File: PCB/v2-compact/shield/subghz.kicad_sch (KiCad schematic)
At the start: 0 parts

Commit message: Schematics: sub-GHz trio sheet (CC1200 + SX1262 + CC1101) + fixes
- 05_SubGHz (A3): CC1200 and SX1262 (bare QFN) with SPI, control, power,
  crystals and decoupling wired; CC1101 as an 8-pin module. Chip-selects come
  from the MCP23S17 (CC1200_CS, SX1262_NSS, CC1101_CSN), SX1262 BUSY direct on
  the C5. RF front-ends (PA/LNA/RFO/RFI -> match -> SMA) flagged for the RF pass.
  Verified: SPI_SCK now reaches all nine SPI devices.
- Fix the Espressif symbol-lib-table path to Windows form (was Git-Bash /d/...).
- Add A3 page support to the generator.
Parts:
- added C80, C81: 10pF, Capacitor_SMD:C_0402_1005Metric, symbol Device:C
- added C82, C83, C86, C87, C88: 100nF, Capacitor_SMD:C_0402_1005Metric, symbol Device:C
- added C84, C85: 12pF, Capacitor_SMD:C_0402_1005Metric, symbol Device:C
- added R80: 56k, Resistor_SMD:R_0402_1005Metric, symbol Device:R
- added U4: CC1101, symbol SnowOwl:CC1101_Module
- added U5: CC1200RHBR, Package_DFN_QFN:QFN-32-1EP_5x5mm_P0.5mm_EP3.45x3.45mm, symbol RF:CC1200
- added U6: SX1262IMLTRT, Package_DFN_QFN:QFN-24-1EP_4x4mm_P0.5mm_EP2.6x2.6mm, symbol RF:SX1262IMLTRT
- added Y60: 40MHz, Crystal:Crystal_SMD_3225-4Pin_3.2x2.5mm, symbol Device:Crystal
- added Y61: 32MHz, Crystal:Crystal_SMD_3225-4Pin_3.2x2.5mm, symbol Device:Crystal
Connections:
- new net +3V3: C82.1, C86.1, C88.1, U4.2 (VCC), U5.1 (VDD_GUARD), U5.12 (DVDD), U5.13 (AVDD_IF), U5.15 (AVDD_RF), U5.22 (AVDD_SYNTH1), U5.25 (AVDD_PFD_CHP), U5.27 (AVDD_SYNTH2), U5.28 (AVDD_XOSC), U5.5 (DVDD), U6.1 (VDD_IN), U6.10 (VBAT), U6.11 (VBAT_IO)
- new net CC1101_CSN: U4.4 (CSN)
- new net CC1101_GDO0: U4.3 (GDO0)
- new net CC1101_GDO2: U4.7 (GDO2)
- new net CC1200_CS: U5.11 (~{CS})
- new net CC1200_GPIO0: U5.10 (GPIO0)
- new net CC1200_GPIO2: U5.4 (GPIO2)
- new net CC1200_GPIO3: U5.3 (GPIO3)
- new net CC1200_RST: U5.2 (~{RESET})
- new net CC12_DCPL_PFD: U5.26 (DCPL_PFD_CHP)
- new net CC12_DCPL_VCO: U5.21 (DCPL_VCO)
- new net CC12_DCPL_XOSC: U5.29 (DCPL_XOSC)
- new net CC12_LNA_N: U5.20 (LNA_N)
- new net CC12_LNA_P: U5.19 (LNA_P)
- new net CC12_LPF0: U5.23 (LPF0)
- new net CC12_LPF1: U5.24 (LPF1)
- new net CC12_PA: U5.17 (PA)
- new net CC12_RBIAS: R80.1, U5.14 (RBIAS)
- new net CC12_TRXSW: U5.18 (TRX_SW)
- new net CC12_XIN: C80.1, U5.30 (XOSC_Q1), Y60.1
- new net CC12_XOUT: C81.1, U5.31 (XOSC_Q2), Y60.2
- new net GND: C80.2, C81.2, C82.2, C83.1, C83.2, C84.2, C85.2, C86.2, C87.1, C87.2, C88.2, R80.2, U4.1 (GND), U5.32 (EXT_XOSC), U5.33 (GND_EP), U5.6 (DCPL), U6.2 (GND), U6.20 (GND), U6.25 (GND), U6.5 (GND), U6.7 (VREG), U6.8 (GND)
- new net SPI_MISO: U4.8 (MISO), U5.9 (SO(GPIO1)), U6.16 (MISO)
- new net SPI_MOSI: U4.6 (MOSI), U5.7 (SI), U6.17 (MOSI)
- new net SPI_SCK: U4.5 (SCK), U5.8 (SCLK), U6.18 (SCK)
- new net SX1262_BUSY: U6.14 (BUSY)
- new net SX1262_DIO1: U6.13 (DIO1)
- new net SX1262_DIO2: U6.12 (DIO2)
- new net SX1262_DIO3: U6.6 (DIO3)
- new net SX1262_NSS: U6.19 (NSS)
- new net SX1262_RST: U6.15 (~{RESET})
- new net SX_DCC: U6.9 (DCC_SW)
- new net SX_RFI_N: U6.22 (RFI_N)
- new net SX_RFI_P: U6.21 (RFI_P)
- new net SX_RFO: U6.23 (RFO)
- new net SX_VR_PA: U6.24 (VR_PA)
- new net SX_XTA: C84.1, U6.3 (XTA), Y61.1
- new net SX_XTB: C85.1, U6.4 (XTB), Y61.2
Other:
- note added: "CC1200 RF: PA/TRX_SW/LNA_P/LNA_N -> balun + match -> SMA1; LPF0/1 + DCPL_* cap values TBD per CC1200 ref design"
- note added: "SX1262 RF: RFO/RFI_P/RFI_N -> match + RF switch -> SMA2; DCC_SW inductor (DCDC) values TBD per SX1262 ref design"
- note removed: "05_Sub-GHz [zone: NORTH edge, 3 slots behind SMAs] CC1101 + CC1200 + SX1262(LoRa), each with crystal + matching, each right behind its own SMA (RF run <10mm). Shared SPI taps the central spine; CS/GDO/DIO/BUSY fan to each."

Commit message: Schematics: cleanup - HTRC110 footprint (SOIC-14), reset pull-ups (CC1200/GPS), RV1106 power flags
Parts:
- added R81: 10k, Resistor_SMD:R_0402_1005Metric, symbol Device:R
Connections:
- net +3V3: now also R81.1
- net CC1200_RST: now also R81.2

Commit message: PCB: import schematic netlists onto both boards (parts placed + nets assigned)
Load every footprint from the schematic into the floorplan-skeleton boards,
place each in its subsystem's zone (grid-spread, back-side sheets flipped), and
assign all nets. Shield: 79 parts, 419 pad-nets, 153 nets. Main: 29 parts,
150 pad-nets, 57 nets. Register the Espressif footprint library; add a
placeholder Core1106 SoM footprint; assign the C5 (Espressif), NEO-M9N (ublox_NEO)
and CC1101 (2x4 header) module footprints.

This is the initial import: every part is on its board with the full ratsnest,
ready for placement refinement and routing.
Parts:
- U4: footprint (none) -> Connector_PinHeader_2.54mm:PinHeader_2x04_P2.54mm_Vertical

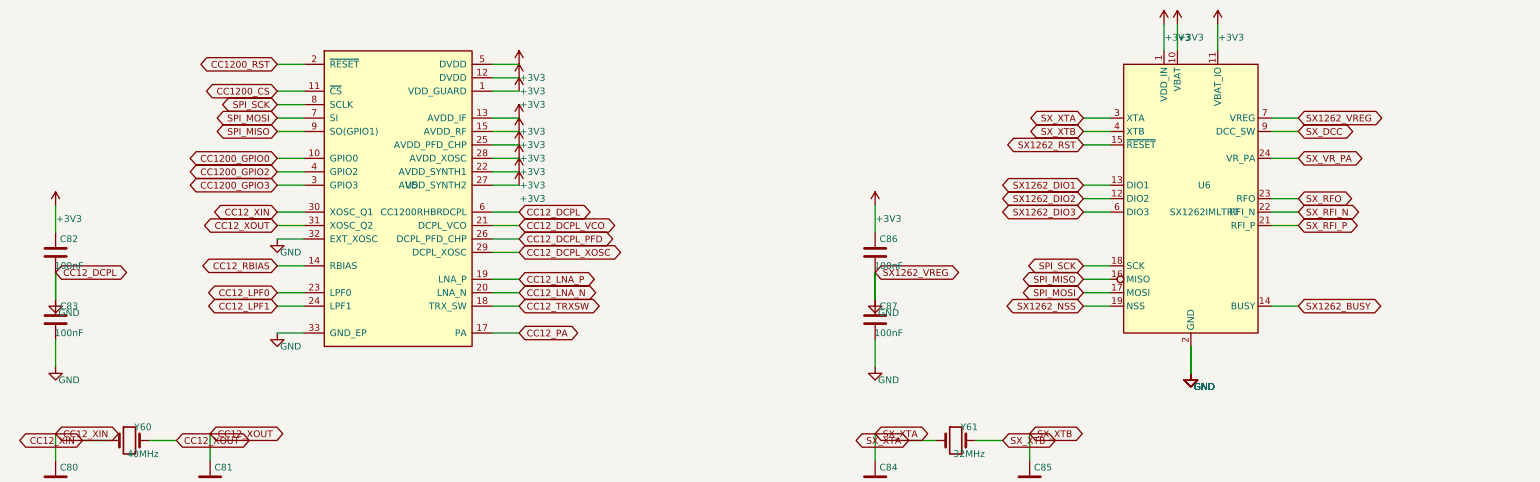
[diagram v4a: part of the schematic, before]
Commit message: Schematic: fix the GND<->CC12_DCPL short (empty ground net) + re-import nets
Root cause of GND having ZERO nodes: in the sub-GHz sheet, C82(+3V3/GND) & C83(CC12_DCPL/GND)
and C86(+3V3/GND) & C87(SX1262_VREG/GND) were each stacked exactly 12mm apart in the same
column. connect()'s 5.08mm wire stubs from the upper cap's GND pin snapped onto the lower
cap's non-GND pin, shorting GND to CC12_DCPL and to SX1262_VREG - which merged every ground
on the board into CC12_DCPL. Moved C83 and C87 off-column to clear positions.

- Verified by KiCad's netlister: GND now 64 comps (shield) / 25 (main), was 0; CC12_DCPL
  back to 2 nodes, SX1262_VREG back to 2.
- Regenerated all sheets, re-exported both netlists, and re-imported the corrected nets onto
  both .kicad_pcb (positions/footprints untouched): shield 433 pad-nets, main 150.
- Hardened the netlist parser's block extractor to skip parens inside quoted strings.
- Also confirmed the regen assigns U30's RV1106 footprint (the earlier empty-footprint netlist
  that made U30 vanish on import was stale).

The ground net can now actually form a plane - unblocks routing. Placement re-verified clean
(0 overlaps, 0 cross-side hole collisions).
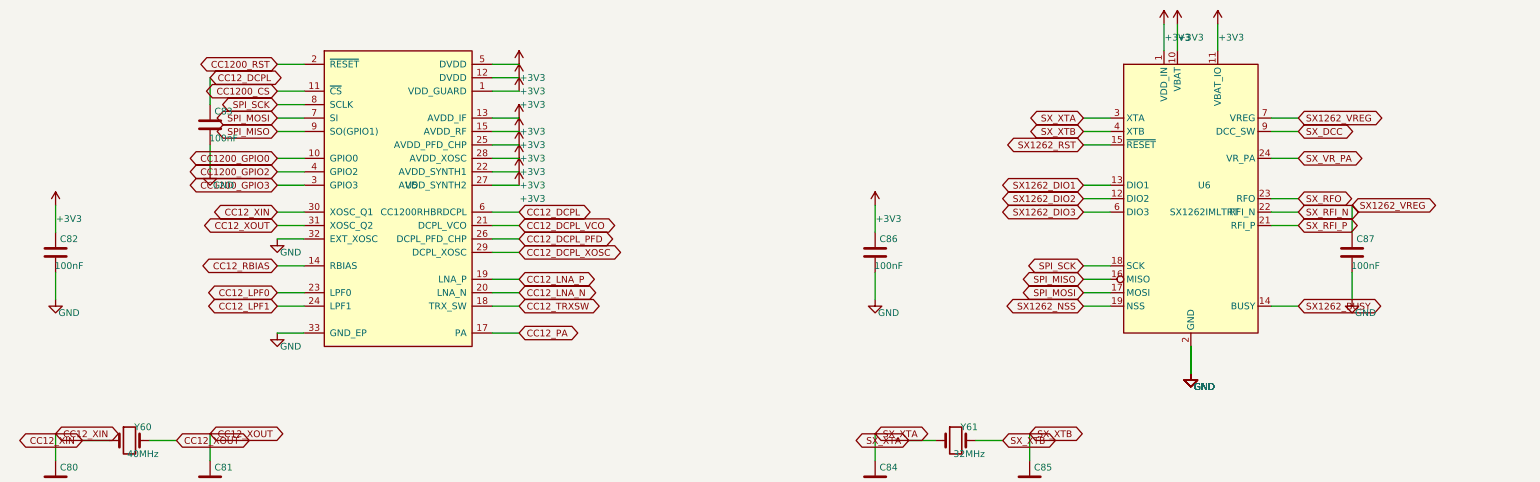
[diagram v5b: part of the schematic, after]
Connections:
- net GND: no longer C83.1, C87.1, U5.6 (DCPL), U6.7 (VREG)
- new net CC12_DCPL: C83.1, U5.6 (DCPL)
- new net SX1262_VREG: C87.1, U6.7 (VREG)
